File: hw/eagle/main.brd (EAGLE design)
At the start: 49.2 x 49.5 mm, 12 parts

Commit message: [ update ] route, wip
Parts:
- moved C1 11.7 mm to (15.2, 38.1), turned to 180 degrees
- moved C3 1.27 mm to (11.4, 44.5), turned to 0 degrees
- moved CON_COIN_HOLDER 1.27 mm to (11.4, 15.2)
- moved COIN_OR_ALT 1.27 mm to (26.7, 40.6)
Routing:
- net COIN_VCC: track 0.00 -> 25.8 mm
- net POW_VCC: track 0.00 -> 6.35 mm
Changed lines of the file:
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@@
 <attribute name="VALUE" x="13.97" y="10.541" size="1.27" layer="27" ratio="10" rot="R180"/>
 </element>
-<element name="C1" library="rcl" package="C1206K" value="100n" x="3.81" y="40.64"/>
+<element name="C1" library="rcl" package="C1206K" value="100n" x="15.24" y="38.1" rot="R180"/>
 <element name="R1" library="resistor" package="R1206" value="1M" x="30.48" y="20.32" rot="R180"/>
 <element name="REED" library="SparkFun" package="1X02" value="" x="46.99" y="12.7" smashed="yes" rot="R270">
@@
 <attribute name="VALUE" x="21.59" y="42.545" size="1.27" layer="27"/>
 </element>
-<element name="COIN_OR_ALT" library="SparkFun" package="1X03" value="" x="26.67" y="41.91" smashed="yes" rot="R180">
-<attribute name="NAME" x="20.3962" y="38.8112" size="0.8128" layer="25" font="vector" ratio="10" rot="R180" align="top-right"/>
-<attribute name="VALUE" x="27.94" y="45.085" size="1.27" layer="27" rot="R180"/>
-</element>
-<element name="C3" library="rcl" package="PANASONIC_F" value="330u" x="12.7" y="44.45" rot="R180"/>
-<element name="CON_COIN_HOLDER" library="SparkFun" package="BATTCOM_20MM_PTH" value="" x="11.43" y="13.97" smashed="yes" rot="MR90">
-<attribute name="NAME" x="20.955" y="14.605" size="0.4064" layer="26" rot="MR90"/>
-<attribute name="VALUE" x="10.795" y="6.985" size="0.4064" layer="28" rot="MR90"/>
+<element name="COIN_OR_ALT" library="SparkFun" package="1X03" value="" x="26.67" y="40.64" smashed="yes" rot="R180">
+<attribute name="NAME" x="20.3962" y="37.5412" size="0.8128" layer="25" font="vector" ratio="10" rot="R180" align="top-right"/>
+<attribute name="VALUE" x="27.94" y="43.815" size="1.27" layer="27" rot="R180"/>
+</element>
+<element name="C3" library="rcl" package="PANASONIC_F" value="330u" x="11.43" y="44.45"/>
+<element name="CON_COIN_HOLDER" library="SparkFun" package="BATTCOM_20MM_PTH" value="" x="11.43" y="15.24" smashed="yes" rot="MR90">
+<attribute name="NAME" x="20.955" y="15.875" size="0.4064" layer="26" rot="MR90"/>
+<attribute name="VALUE" x="10.795" y="8.255" size="0.4064" layer="28" rot="MR90"/>
 </element>
 </elements>
@@
 <contactref element="VCC_SWITCH" pad="1"/>
 <contactref element="COIN_OR_ALT" pad="2"/>
-<wire x1="24.13" y1="41.91" x2="22.86" y2="45.72" width="0" layer="19" extent="1-1"/>
+<wire x1="22.86" y1="45.72" x2="22.86" y2="43.18" width="0.4064" layer="1"/>
+<wire x1="22.86" y1="43.18" x2="24.13" y2="43.18" width="0.4064" layer="1"/>
+<wire x1="24.13" y1="43.18" x2="24.13" y2="40.64" width="0.4064" layer="1"/>
 </signal>
 <signal name="POW_VCC_EN">
@@
 <contactref element="C3" pad="+"/>
 <contactref element="CON_COIN_HOLDER" pad="1"/>
-<wire x1="9.15" y1="44.45" x2="21.59" y2="41.91" width="0" layer="19" extent="1-1"/>
-<wire x1="2.31" y1="40.64" x2="9.15" y2="44.45" width="0" layer="19" extent="1-1"/>
-<wire x1="11.43" y1="33.97" x2="9.15" y2="44.45" width="0" layer="19" extent="1-1"/>
+<wire x1="11.43" y1="35.24" x2="19.05" y2="35.24" width="0.4064" layer="1"/>
+<wire x1="19.05" y1="35.24" x2="19.05" y2="38.1" width="0.4064" layer="1"/>
+<wire x1="19.05" y1="38.1" x2="19.05" y2="40.64" width="0.4064" layer="1"/>
+<wire x1="19.05" y1="40.64" x2="19.05" y2="44.45" width="0.4064" layer="1"/>
+<wire x1="21.59" y1="40.64" x2="19.05" y2="40.64" width="0.4064" layer="1"/>
+<wire x1="19.05" y1="44.45" x2="14.98" y2="44.45" width="0.4064" layer="1"/>
+<wire x1="16.74" y1="38.1" x2="19.05" y2="38.1" width="0.4064" layer="1"/>
 </signal>
 <signal name="ALT_VCC">

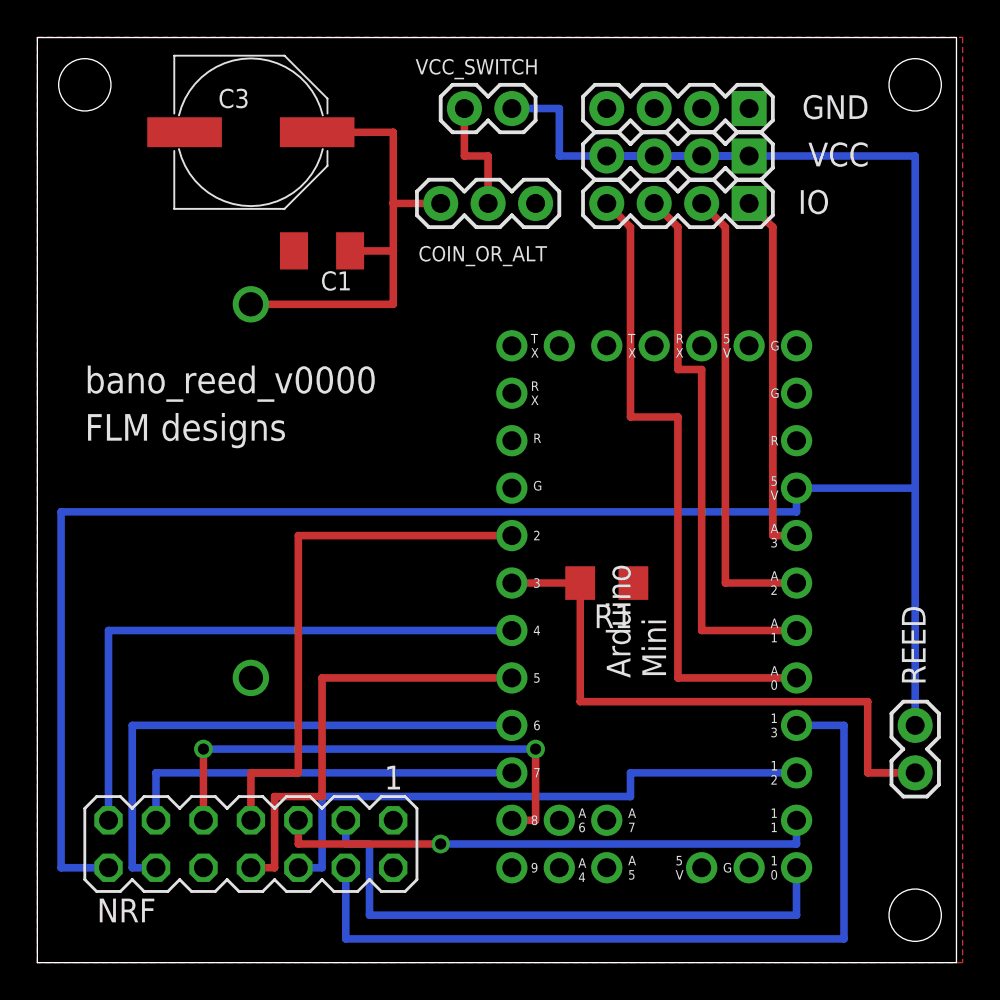
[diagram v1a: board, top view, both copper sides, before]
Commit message: [ update ] route, done. footprints to be checked
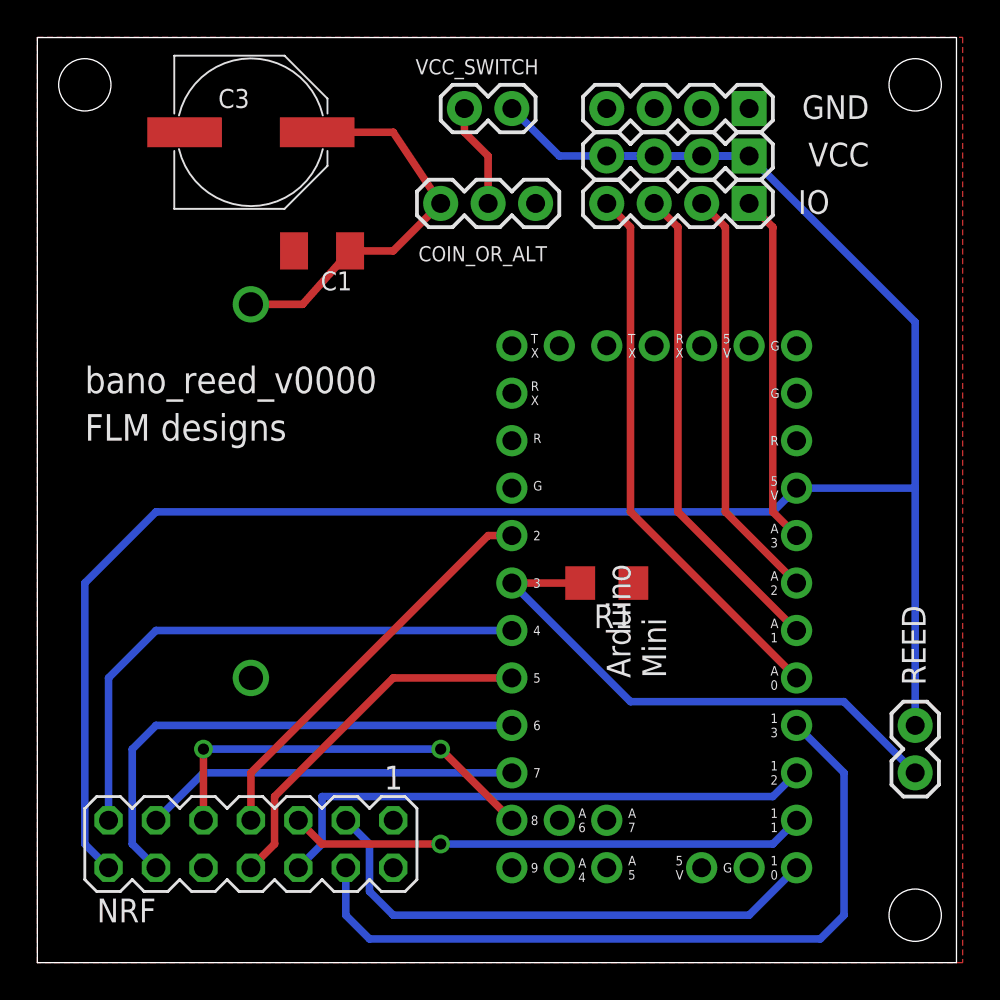
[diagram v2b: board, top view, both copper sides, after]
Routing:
- net POW_VCC_EN: track 130.8 -> 117.9 mm
- net NRF_DR: track 29.2 -> 21.8 mm
- net UC_PORTC0: track 34.8 -> 29.6 mm
- net NRF_CD: track 26.7 -> 21.9 mm
- net COIN_VCC: track 25.8 -> 21.1 mm
- net NRF_AM: track 24.1 -> 19.7 mm
- net UC_PORTC1: track 29.7 -> 26.0 mm
- net NRF_SCK: track 44.5 -> 41.5 mm
- net NRF_CSN: track 31.7 -> 28.8 mm
- net REED_EN: track 31.8 -> 29.5 mm
- net UC_PORTC2: track 24.7 -> 22.4 mm
- net NRF_TXEN: track 31.8 -> 30.3 mm
- net NRF_MOSI: track 29.2 -> 27.7 mm
- net NRF_MISO: track 31.7 -> 30.3 mm
- net NRF_CE: track 29.2 -> 27.7 mm
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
